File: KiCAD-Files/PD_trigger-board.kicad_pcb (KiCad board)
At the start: 2 copper layers, 24 parts, among them J1 USB_C_Receptacle_USB2.0_14P, J10 15V, J11 18V, J2 Conn_01x03, J3 Conn_01x03, J4 VOUT, J5 5V, J6 5V, J7 5V, J8 9V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

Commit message: start routing
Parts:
- moved J6 97.5 mm to (129.8, 95.3), turned to 90 degrees
- moved J5 92.3 mm to (129.8, 91.2), turned to 90 degrees
- moved J4 74.4 mm to (142.2, 104.7), turned to 180 degrees
- moved R2 62.6 mm to (135.6, 95.3)
- moved R4 56.4 mm to (141.2, 88.5), turned to -90 degrees
- moved R5 54.7 mm to (143.3, 85.7)
- moved R6 54.6 mm to (143.3, 89.7)
- moved R7 54.5 mm to (143.3, 93.8)
- moved R8 54.4 mm to (143.3, 97.8)
- moved C1 17.9 mm to (133.1, 87.4), turned to 90 degrees
- moved R1 16.5 mm to (134.6, 87.9), turned to -90 degrees
- moved J11 16.4 mm to (146.6, 97.8)
- moved J9 15.0 mm to (146.6, 89.7)
- moved J10 14.9 mm to (146.6, 93.8)
- moved J7 14.8 mm to (146.6, 81.6)
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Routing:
- net VSET: track 0.00 -> 19.3 mm, vias 0 -> 1
- net VBUS: track 0.00 -> 7.21 mm, vias 0 -> 2
- net VOUT: track 0.00 -> 6.59 mm
- net Net-(J8-Pin_1): track 0.00 -> 2.84 mm, vias 0 -> 1
- net Net-(J10-Pin_1): track 0.00 -> 2.84 mm, vias 0 -> 1
- net Net-(J9-Pin_1): track 0.00 -> 2.84 mm, vias 0 -> 1
- net Net-(J11-Pin_1): track 0.00 -> 2.84 mm, vias 0 -> 1

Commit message: Routin fertig
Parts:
- added U2: SI4459ADY-T1-GE3, blinkyparts:SO_ADY-T1-GE3_VIS, F.Cu at (139.1, 96.1)
- moved J5 15.5 mm to (145.0, 88.2)
- moved J6 15.4 mm to (145.0, 93.0)
- moved J7 13.6 mm to (132.9, 82.5), turned to -90 degrees
- moved J8 13.6 mm to (133.0, 86.4), turned to -90 degrees
- moved J9 13.6 mm to (133.0, 90.3), turned to -90 degrees
- moved J10 13.6 mm to (133.0, 94.1), turned to -90 degrees
- moved J11 13.6 mm to (133.0, 97.9), turned to -90 degrees
- moved R2 10.5 mm to (145.1, 90.6)
- moved R3 9.68 mm to (142.9, 95.7), turned to 180 degrees
- moved C1 9.32 mm to (142.3, 86.3)
- moved R4 8.42 mm to (142.9, 96.7), turned to 0 degrees
- moved R8 7.93 mm to (135.3, 97.4), turned to -90 degrees
- moved R7 7.89 mm to (135.4, 93.6), turned to -90 degrees
- moved R5 7.89 mm to (135.4, 85.9), turned to -90 degrees
- moved R6 7.89 mm to (135.4, 89.8), turned to -90 degrees
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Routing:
- net D+: track 0.00 -> 42.7 mm, vias 0 -> 3
- net D-: track 0.00 -> 39.3 mm, vias 0 -> 1
- net VOUT: track 6.59 -> 33.8 mm, vias 0 -> 3
- net SCL: track 0.00 -> 26.4 mm, vias 0 -> 1
- net SDA: track 0.00 -> 25.0 mm, vias 0 -> 1
- net VBUS: track 7.21 -> 28.7 mm, vias 2 -> 6
- net CC1: track 0.00 -> 11.0 mm, vias 0 -> 2
- net GATE: track 0.00 -> 10.8 mm, vias 0 -> 2
- net ISET: track 0.00 -> 9.27 mm
- net Net-(U2-G): track 0.00 -> 7.92 mm
- net CC2: track 0.00 -> 4.87 mm
- net VSET: track 19.3 -> 22.6 mm, vias 1 -> 0
- net Net-(U1-VIN): track 0.00 -> 3.08 mm
- net GND: track 0.00 -> 3.08 mm
- net Net-(J6-Pin_1): track 0.00 -> 2.63 mm
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- added copper zone on B.Cu, net GND
- added copper zone on F.Cu, net GND
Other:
- board text added: "J5: 1.25A J6 + R2: 4,53 - 1,50A 7,5k - 1,75A 10,5k - 2,00A 13,7k - 2,25A 16,5k - 2,50A 19,6k - 2,75A 22,6k - 3,00A open - 3,25A"
- board text added: "J7: 5V J8: 9V J9: 12V J10: 15V J11: 18V"

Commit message: changed some routing
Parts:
- moved C1 1.25 mm to (142.2, 87.5), turned to -90 degrees
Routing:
- net VOUT: track 33.8 -> 3.50 mm, vias 3 -> 7
- net VBUS: track 28.7 -> 13.7 mm
- net VSET: track 22.6 -> 26.3 mm
- net D-: track 39.3 -> 40.7 mm
- net SCL: track 26.4 -> 25.9 mm
- added copper zone on B.Cu, net VBUS
- added copper zone on B.Cu, net VOUT
- added copper zone on F.Cu, net VOUT
- removed copper zone on B.Cu, net GND
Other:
- board outline added: 21 x 37.1 mm

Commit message: Silkscreen fertig
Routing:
- net D-: track 40.7 -> 39.7 mm
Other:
- board size 21 x 37.1 mm -> 21 x 37.8 mm
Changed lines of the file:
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@@
 		(tags "resistor")
 		(property "Reference" "R5"
-			(at -0.39 -1.17 90)
+			(at -1.6 0 90)
 			(layer "F.SilkS")
 			(effects
 				(font
-					(size 1 1)
-					(thickness 0.15)
+					(size 0.8 0.8)
+					(thickness 0.1)
 				)
 			)
@@
 		(tags "resistor")
 		(property "Reference" "R7"
-			(at -1.79 -0.125 90)
+			(at -1.6 0 90)
 			(layer "F.SilkS")
 			(effects
 				(font
-					(size 1 1)
-					(thickness 0.15)
+					(size 0.8 0.8)
+					(thickness 0.1)
 				)
 			)
@@
 		(tags "usb usb-c 2.0 pd")
 		(property "Reference" "J1"
-			(at -0.107 0.022 0)
+			(at -6 0 0)
 			(layer "F.SilkS")
 			(effects
 				(font
-					(size 1 1)
-					(thickness 0.15)
+					(size 0.8 0.8)
+					(thickness 0.1)
 				)
 			)
@@
 		(tags "resistor")
 		(property "Reference" "R6"
-			(at -1.79 -0.025 90)
+			(at -1.6 0 90)
 			(layer "F.SilkS")
 			(effects
 				(font
-					(size 1 1)
-					(thickness 0.15)
+					(size 0.8 0.8)
+					(thickness 0.1)
 				)
 			)
@@
 		(tags "resistor")
 		(property "Reference" "R3"
-			(at -2.1 0.1 0)
+			(at -1.6 0 0)
 			(layer "F.SilkS")
 			(effects
 				(font
-					(size 1 1)
-					(thickness 0.15)
+					(size 0.8 0.8)
+					(thickness 0.1)
 				)
 			)
@@
 		(tags "Through hole pin header THT 1x03 2.54mm single row")
 		(property "Reference" "J2"
-			(at 2.194 4.32 180)
+			(at 1.9 2.54 180)
 			(layer "F.SilkS")
 			(effects
 				(font
-					(size 1 1)
-					(thickness 0.15)
+					(size 0.8 0.8)
+					(thickness 0.1)
 				)
 			)
@@
 		(tags "resistor")
 		(property "Reference" "R1"
-			(at -1.582 0.2 180)
+			(at -1.6 0 90)
 			(layer "F.SilkS")
 			(effects
 				(font
-					(size 1 1)
-					(thickness 0.15)
+					(size 0.8 0.8)
+					(thickness 0.1)
 				)
 			)
@@
 			(effects
 				(font
-					(size 1 1)
-					(thickness 0.15)
+					(size 0.8 0.8)
+					(thickness 0.1)
 				)
 			)
@@
 			(effects
 				(font
-					(size 1 1)
-					(thickness 0.15)
+					(size 0.8 0.8)
+					(thickness 0.1)
 				)
 			)
@@
 			(effects
 				(font
-					(size 1 1)
-					(thickness 0.15)
+					(size 0.8 0.8)
+					(thickness 0.1)
 				)
 			)
@@
 		(tags "resistor")
 		(property "Reference" "R2"
-			(at 0 -1.17 0)
+			(at 1.6 0 0)
 			(layer "F.SilkS")
 			(effects
 				(font
-					(size 1 1)
-					(thickness 0.15)
+					(size 0.8 0.8)
+					(thickness 0.1)
 				)
 			)
@@
 		(tags "SI4459ADY-T1-GE3 ")
 		(property "Reference" "U2"
-			(at 0 0 90)
+			(at -1.8 -3.4 90)
 			(unlocked yes)
 			(layer "F.SilkS")
 			(effects
 				(font
-					(size 1 1)
-					(thickness 0.15)
+					(size 0.8 0.8)
+					(thickness 0.1)
 				)
 			)
@@
 			(layer "F.Fab")
 		)
-		(fp_text user "*"
-			(at -0.982 1.3 -90)
-			(unlocked yes)
-			(layer "F.SilkS")
-			(effects
-				(font
-					(size 0.75 0.75)
-					(thickness 0.1)
-				)
-			)
-		)
-		(fp_text user "*"
-			(at 1.318 0.5 90)
-			(unlocked yes)
-			(layer "F.SilkS")
-			(effects
-				(font
-					(size 0.75 0.75)
-					(thickness 0.1)
-				)
-			)
-		)
 		(fp_text user "${REFERENCE}"
 			(at 0 0 -90)
@@
 		(tags "terminal block bornier2")
 		(property "Reference" "J4"
-			(at -3.62 -0.4 0)
-			(layer "B.SilkS")
+			(at -3.6 0 0)
+			(layer "F.SilkS")
 			(effects
 				(font
-					(size 1 1)
+					(size 0.8 0.8)
 					(thickness 0.15)
 				)
@@
 		(tags "capacitor")
 		(property "Reference" "C2"
-			(at -0.06 1.372 0)
+			(at 0 1.2 0)
 			(layer "F.SilkS")
 			(effects
 				(font
-					(size 1 1)
-					(thickness 0.15)
+					(size 0.8 0.8)
+					(thickness 0.1)
 				)
 			)
@@
 		(tags "resistor")
 		(property "Reference" "R8"
-			(at -1.9 -0.155 90)
+			(at -1.6 0 90)
 			(layer "F.SilkS")
 			(effects
 				(font
-					(size 1 1)
-					(thickness 0.15)
+					(size 0.8 0.8)
+					(thickness 0.1)
 				)
 			)
@@
 		(tags "Through hole pin header THT 1x02 2.54mm single row")
 		(property "Reference" "J5"
-			(at 2.29 3.629 90)
+			(at 2.5 3.6 90)
 			(layer "F.SilkS")
 			(effects
 				(font
-					(size 0.75 0.75)
+					(size 0.8 0.8)
 					(thickness 0.1)
 				)
@@
 		(tags "Through hole pin header THT 1x02 2.54mm single row")
 		(property "Reference" "J8"
-			(at 0 3.85 -90)
+			(at 0 3.85 270)
 			(layer "B.SilkS")
 			(effects
 				(font
-					(size 1 1)
-					(thickness 0.15)
+					(size 0.8 0.8)
+					(thickness 0.1)
 				)
 			)
@@
 		(tags "DFN 0.5")
 		(property "Reference" "U1"
-			(at 0 -2.575 90)
+			(at 0 -2.4 90)
 			(layer "F.SilkS")
 			(effects
 				(font
-					(size 1 1)
-					(thickness 0.15)
+					(size 0.8 0.8)
+					(thickness 0.1)
 				)
 			)
@@
 		(tags "resistor")
 		(property "Reference" "R4"
-			(at 2.2 0.3 0)
+			(at 1.6 0 0)
 			(layer "F.SilkS")
 			(effects
 				(font
-					(size 1 1)
-					(thickness 0.15)
+					(size 0.8 0.8)
+					(thickness 0.1)
 				)
 			)
@@
 		(tags "capacitor")
 		(property "Reference" "C4"
-			(at 0 1.492 0)
+			(at 0 1.2 0)
 			(layer "F.SilkS")
 			(effects
 				(font
-					(size 1 1)
-					(thickness 0.15)
+					(size 0.8 0.8)
+					(thickness 0.1)
 				)
 			)
@@
 		(tags "capacitor")
 		(property "Reference" "C3"
-			(at 0 1.382 0)
+			(at 0 1.2 0)
 			(layer "F.SilkS")
 			(effects
 				(font
-					(size 1 1)
-					(thickness 0.15)
+					(size 0.8 0.8)
+					(thickness 0.1)
 				)
 			)
@@
 		(tags "Through hole pin header THT 1x02 2.54mm single row")
 		(property "Reference" "J6"
-			(at 1.1 3.8 90)
+			(at 2.5 3.6 90)
 			(layer "F.SilkS")
 			(effects
 				(font
-					(size 1 1)
-					(thickness 0.15)
+					(size 0.8 0.8)
+					(thickness 0.1)
 				)
 			)
@@
 		(tags "Through hole pin header THT 1x03 2.54mm single row")
 		(property "Reference" "J3"
-			(at -1.894 0.8 180)
-			(layer "B.SilkS")
+			(at -1.9 2.54 180)
+			(layer "F.SilkS")
 			(effects
 				(font
-					(size 1 1)
-					(thickness 0.15)
+					(size 0.8 0.8)
+					(thickness 0.1)
 				)
 			)
@@
 			(effects
 				(font
-					(size 1 1)
-					(thickness 0.15)
+					(size 0.8 0.8)
+					(thickness 0.1)
 				)
 				(justify mirror)
@@
 		(tags "capacitor")
 		(property "Reference" "C1"
-			(at 0.6595 1.6525 360)
+			(at -2.2 0 90)
 			(layer "F.SilkS")
 			(effects
 				(font
-					(size 1 1)
-					(thickness 0.15)
+					(size 0.8 0.8)
+					(thickness 0.1)
 				)
 			)
@@
 	)
 	(gr_line
-		(start 148 76.4)
-		(end 130 76.4)
+		(start 148 75.7)
+		(end 130 75.7)
 		(stroke
 			(width 0.05)
@@
 	(gr_line
 		(start 149.5 112)
-		(end 149.5 77.9)
+		(end 149.46066 77.16066)
 		(stroke
 			(width 0.05)
@@
 	)
 	(gr_line
-		(start 128.5 77.9)
+		(start 128.539566 77.16066)
 		(end 128.5 112)
 		(stroke
@@
 	)
 	(gr_arc
-		(start 148 76.4)
-		(mid 149.06066 76.83934)
-		(end 149.5 77.9)
+		(start 148 75.7)
+		(mid 149.032843 76.127817)
+		(end 149.46066 77.16066)
 		(stroke
 			(width 0.05)
@@
 	)
 	(gr_arc
-		(start 128.5 77.9)
-		(mid 128.93934 76.83934)
-		(end 130 76.4)
+		(start 128.539566 77.16066)
+		(mid 128.967317 76.127977)
+		(end 130 75.700226)
 		(stroke
 			(width 0.05)
@@
 	)
 	(gr_text " J7:  5V\n J8:  9V\n J9: 12V\nJ10: 15V\nJ11: 18V"
-		(at 140.3 89.8 0)
+		(at 139.7 99.1 0)
 		(layer "B.SilkS")
 		(effects
 			(font
-				(size 1 1)
+				(size 0.8 0.8)
 				(thickness 0.1)
 			)
@@
 	)
 	(gr_text "J5:     1.25A\nJ6 + R2:\n 4,53 - 1,50A\n 7,5k - 1,75A\n10,5k - 2,00A\n13,7k - 2,25A\n16,5k - 2,50A\n19,6k - 2,75A\n22,6k - 3,00A\nopen  - 3,25A"
-		(at 148.6 109.5 0)
+		(at 143.6 92.8 0)
 		(layer "B.SilkS")
 		(effects
 			(font
-				(size 0.75 0.75)
+				(size 0.8 0.8)
 				(thickness 0.1)
 			)
@@
 		(width 0.2)
 		(layer "B.Cu")
-		(net 4)
-	)
-	(segment
-		(start 143.4 100.5)
-		(end 144.12 101.22)
-		(width 0.2)
-		(layer "B.Cu")

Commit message: Silkscreen update
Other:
- board text added: "shop.blinkyparts.com CC-BY-SA 4.0"
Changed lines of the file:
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@@
 		(tags "terminal block bornier2")
 		(property "Reference" "J4"
-			(at -3.6 0 0)
+			(at -3.6 -3.5 0)
 			(layer "F.SilkS")
 			(effects
@@
 		)
 	)
+	(gr_text "shop.blinkyparts.com\nCC-BY-SA 4.0"
+		(at 148.7 108.1 90)
+		(layer "F.SilkS")
+		(effects
+			(font
+				(size 0.8 0.8)
+				(thickness 0.1)
+			)
+			(justify left bottom)
+		)
+	)

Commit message: added gerber files and made minor modifications
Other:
- board text added: "J5: 1.25A J6 + R2: 4,53k - 1,50A 7,5k - 1,75A 10,5k - 2,00A 13,7k - 2,25A 16,5k - 2,50A 19,6k - 2,75A 22,6k - 3,00A open - 3,25A"
- board text added: "blinkyparts GmbH Egerstr. 9, RGB CC-BY-SA 4.0"
- board text removed: "J5: 1.25A J6 + R2: 4,53 - 1,50A 7,5k - 1,75A 10,5k - 2,00A 13,7k - 2,25A 16,5k - 2,50A 19,6k - 2,75A 22,6k - 3,00A open - 3,25A"
- board text removed: "shop.blinkyparts.com CC-BY-SA 4.0"

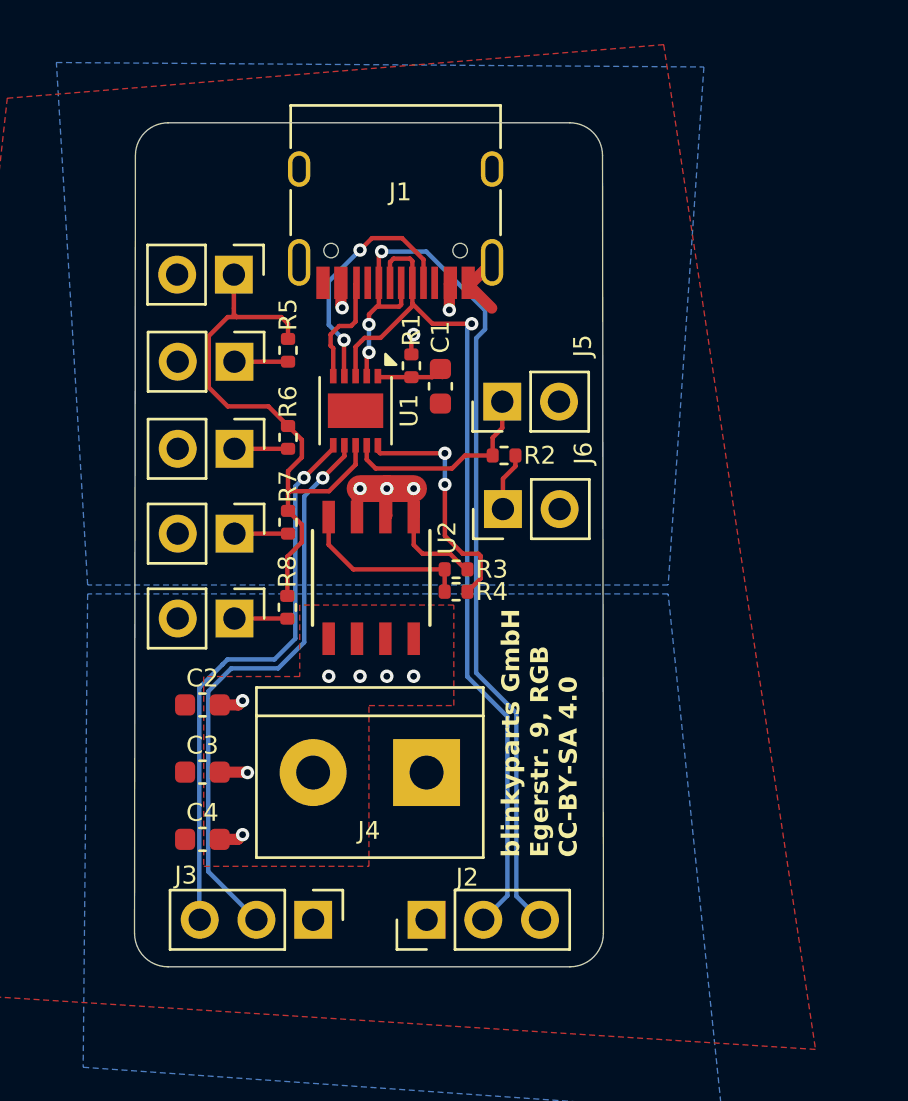
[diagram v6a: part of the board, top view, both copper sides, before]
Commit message: first draft of new layout
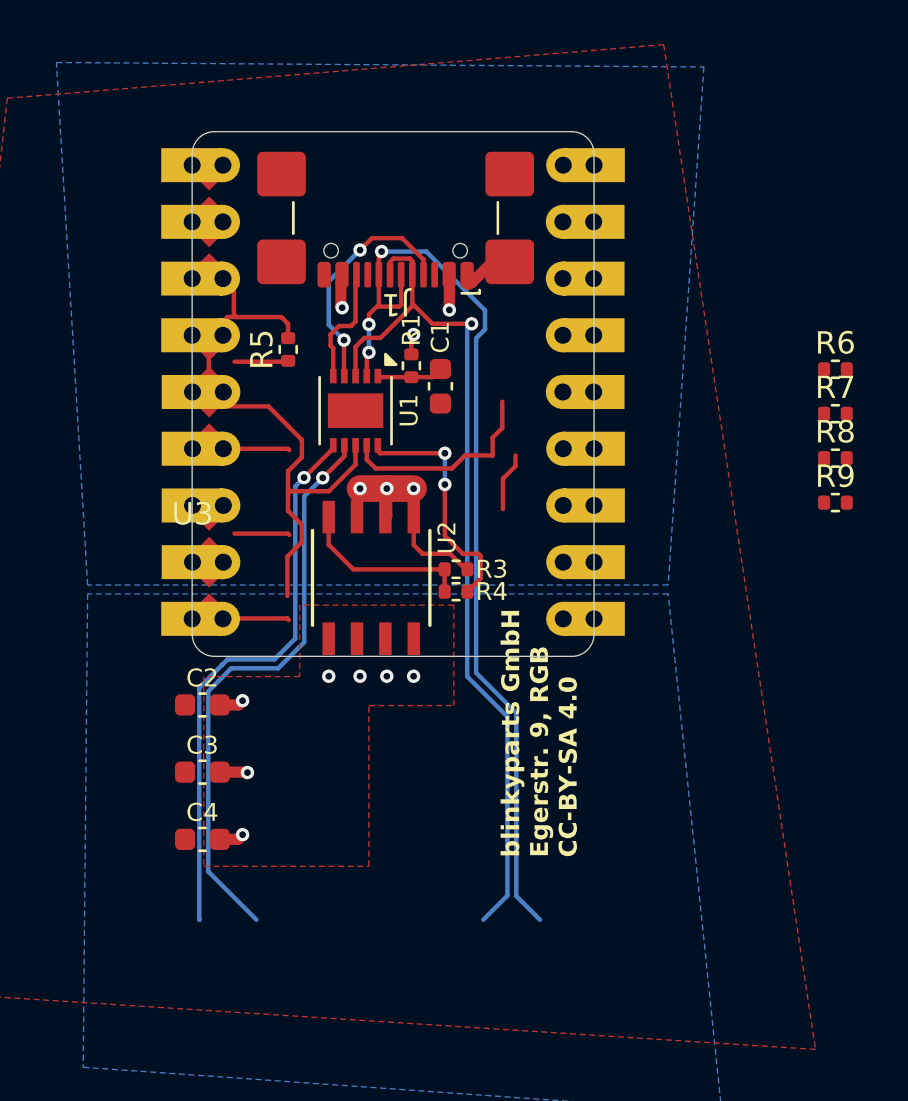
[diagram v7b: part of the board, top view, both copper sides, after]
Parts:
- removed J10: 15V, Connector_PinHeader_2.54mm:PinHeader_1x02_P2.54mm_Vertical
- removed J11: 18V, Connector_PinHeader_2.54mm:PinHeader_1x02_P2.54mm_Vertical
- removed J2, J3: Conn_01x03, Connector_PinHeader_2.54mm:PinHeader_1x03_P2.54mm_Vertical
- removed J4: VOUT, TerminalBlock:TerminalBlock_bornier-2_P5.08mm
- removed J5, J6, J7: 5V, Connector_PinHeader_2.54mm:PinHeader_1x02_P2.54mm_Vertical
- removed J8: 9V, Connector_PinHeader_2.54mm:PinHeader_1x02_P2.54mm_Vertical
- removed J9: 12V, Connector_PinHeader_2.54mm:PinHeader_1x02_P2.54mm_Vertical
- removed R2: 14k, Resistor_SMD:R_0402_1005Metric
- added R9: 22.6k, Resistor_SMD:R_0402_1005Metric, F.Cu at (159.9, 92.7)
- added U3: ESP32-S3-mini_pinprofile, blinkyparts:ESP32-S3-Zero, F.Cu at (131.1, 93.6)
- C2, C3, C4: value C -> 4.7uF 35V
- J1: value USB_C_Receptacle_USB2.0_14P -> USB_C_Receptacle_USB3.0_12P; footprint Connector_USB:USB_C_Receptacle_HRO_TYPE-C-31-M-12 -> Connector_USB:USB_C_Receptacle_GCT_USB4110
- R5: value 6k -> 6.04k
- moved R8 25.4 mm to (159.9, 90.7), turned to 0 degrees
- moved R7 25.0 mm to (159.9, 88.7), turned to 0 degrees
- moved R6 24.7 mm to (159.9, 86.7), turned to 0 degrees
- turned R5 to 90 degrees
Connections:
- U1 pad 9: ISET -> Net-(U1-ISET)
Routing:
- net Net-(U1-ISET): track 0.00 -> 9.27 mm
- net ISET: track 9.27 -> 0.00 mm
- net (no net): track 0.00 -> 5.12 mm
- net Net-(J6-Pin_1): track 2.63 -> 0.00 mm
- net Net-(U3-SET_12V): track 2.48 -> 0.00 mm
- net Net-(U3-SET_18V): track 2.46 -> 0.00 mm
- net VSET: track 26.3 -> 28.7 mm
- net Net-(U3-SET_9V): track 2.40 -> 0.00 mm
- net GND: track 3.20 -> 3.98 mm
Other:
- board size 21 x 37.8 mm -> 18 x 23.5 mm
- board text removed: "J5: 1.25A J6 + R2: 4,53k - 1,50A 7,5k - 1,75A 10,5k - 2,00A 13,7k - 2,25A 16,5k - 2,50A 19,6k - 2,75A 22,6k - 3,00A open - 3,25A"
